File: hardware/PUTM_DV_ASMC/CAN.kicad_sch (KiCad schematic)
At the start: 30 parts, among them U5 ADM3057ExRW, U6 ADM3057ExRW

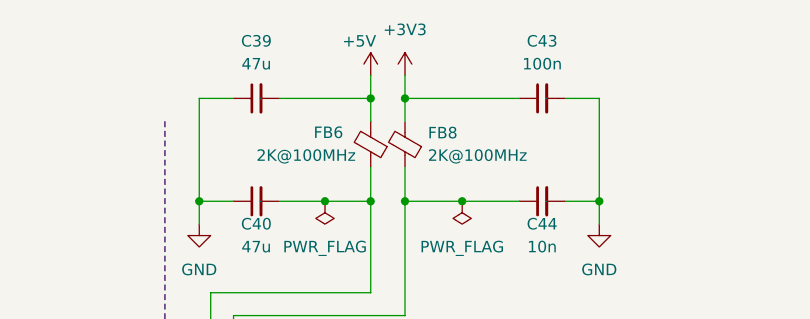
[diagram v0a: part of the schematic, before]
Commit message: update spi schema
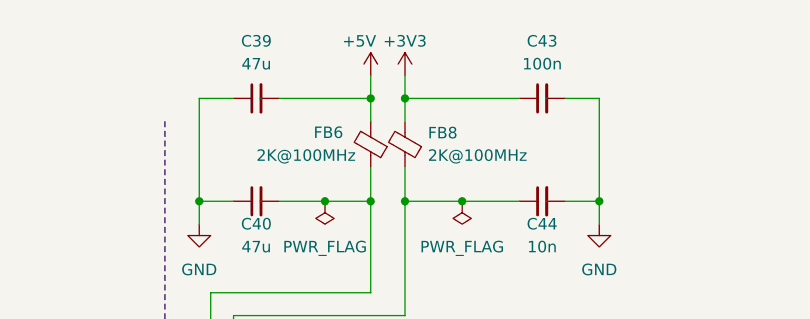
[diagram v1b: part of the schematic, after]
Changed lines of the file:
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@@
 		(in_pos_files yes)
 		(dnp no)
-		(fields_autoplaced yes)
 		(property "Reference" "#PWR042"
 			(at 143.51 22.86 0)
@@
 		)
 		(property "Value" "+3V3"
-			(at 143.51 13.97 0)
+			(at 143.51 15.24 0)
 			(show_name no)
 			(do_not_autoplace no)
